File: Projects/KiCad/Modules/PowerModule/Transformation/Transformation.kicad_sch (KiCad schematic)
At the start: 46 parts, among them J1 Conn_01x02_Pin, J2 Conn_01x02_Pin, J3 Conn_01x02_Pin, J4 Conn_01x02_Pin, Q1 TJ8S06M3L, Q2 TJ8S06M3L, Q3 TJ8S06M3L, SW1 SW_SPDT, U1 NJM7812SDL1, U2 NJM7812SDL1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

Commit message: チップ積層セラミックコンデンサをSMD1608に変更
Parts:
- C2, C6, C9: footprint Capacitor_SMD:C_0805_2012Metric_Pad1.18x1.45mm_HandSolder -> Capacitor_SMD:C_0603_1608Metric_Pad1.08x0.95mm_HandSolder
- C3, C4, C5: value 0.33μF -> 10μF; footprint Capacitor_SMD:C_0805_2012Metric_Pad1.18x1.45mm_HandSolder -> Capacitor_SMD:C_0603_1608Metric_Pad1.08x0.95mm_HandSolder
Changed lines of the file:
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@@
       (effects (font (size 1.27 1.27)) (justify left))
     )
-    (property "Value" "0.33μF" (at 52.07 133.985 0)
-      (effects (font (size 1.27 1.27)) (justify left))
-    )
-    (property "Footprint" "Capacitor_SMD:C_0805_2012Metric_Pad1.18x1.45mm_HandSolder" (at 49.2252 135.89 0)
+    (property "Value" "10μF" (at 52.07 133.985 0)
+      (effects (font (size 1.27 1.27)) (justify left))
+    )
+    (property "Footprint" "Capacitor_SMD:C_0603_1608Metric_Pad1.08x0.95mm_HandSolder" (at 49.2252 135.89 0)
       (effects (font (size 1.27 1.27)) hide)
     )
@@
       (effects (font (size 1.27 1.27)) (justify left))
     )
-    (property "Footprint" "Capacitor_SMD:C_0805_2012Metric_Pad1.18x1.45mm_HandSolder" (at 74.6252 135.89 0)
+    (property "Footprint" "Capacitor_SMD:C_0603_1608Metric_Pad1.08x0.95mm_HandSolder" (at 74.6252 135.89 0)
       (effects (font (size 1.27 1.27)) hide)
     )
@@
       (effects (font (size 1.27 1.27)) (justify left))
     )
-    (property "Value" "0.33μF" (at 102.87 133.985 0)
-      (effects (font (size 1.27 1.27)) (justify left))
-    )
-    (property "Footprint" "Capacitor_SMD:C_0805_2012Metric_Pad1.18x1.45mm_HandSolder" (at 100.0252 135.89 0)
+    (property "Value" "10μF" (at 102.87 133.985 0)
+      (effects (font (size 1.27 1.27)) (justify left))
+    )
+    (property "Footprint" "Capacitor_SMD:C_0603_1608Metric_Pad1.08x0.95mm_HandSolder" (at 100.0252 135.89 0)
       (effects (font (size 1.27 1.27)) hide)
     )
@@
       (effects (font (size 1.27 1.27)) (justify left))
     )
-    (property "Value" "0.33μF" (at 151.13 133.985 0)
-      (effects (font (size 1.27 1.27)) (justify left))
-    )
-    (property "Footprint" "Capacitor_SMD:C_0805_2012Metric_Pad1.18x1.45mm_HandSolder" (at 148.2852 135.89 0)
+    (property "Value" "10μF" (at 151.13 133.985 0)
+      (effects (font (size 1.27 1.27)) (justify left))
+    )
+    (property "Footprint" "Capacitor_SMD:C_0603_1608Metric_Pad1.08x0.95mm_HandSolder" (at 148.2852 135.89 0)
       (effects (font (size 1.27 1.27)) hide)
     )
@@
       (effects (font (size 1.27 1.27)) (justify left))
     )
-    (property "Footprint" "Capacitor_SMD:C_0805_2012Metric_Pad1.18x1.45mm_HandSolder" (at 173.6852 135.89 0)
+    (property "Footprint" "Capacitor_SMD:C_0603_1608Metric_Pad1.08x0.95mm_HandSolder" (at 173.6852 135.89 0)
       (effects (font (size 1.27 1.27)) hide)
     )
@@
       (effects (font (size 1.27 1.27)) (justify left))
     )
-    (property "Footprint" "Capacitor_SMD:C_0805_2012Metric_Pad1.18x1.45mm_HandSolder" (at 125.4252 135.89 0)
-      (effects (font (size 1.27 1.27)) hide)
-    )
+    (property "Footprint" "Capacitor_SMD:C_0603_1608Metric_Pad1.08x0.95mm_HandSolder" (at 125.4252 135.89 0)
+      (effects (font (size 1.27 1.27)) hide)
+    )

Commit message: 抵抗の在庫に合わせてサイズを変更
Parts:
- R1, R2: footprint Resistor_SMD:R_0603_1608Metric_Pad0.98x0.95mm_HandSolder -> Resistor_SMD:R_0805_2012Metric_Pad1.20x1.40mm_HandSolder
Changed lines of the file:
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@@
       (effects (font (size 1.27 1.27)) (justify left))
     )
-    (property "Footprint" "Resistor_SMD:R_0603_1608Metric_Pad0.98x0.95mm_HandSolder" (at 55.118 55.88 90)
+    (property "Footprint" "Resistor_SMD:R_0805_2012Metric_Pad1.20x1.40mm_HandSolder" (at 55.118 55.88 90)
       (effects (font (size 1.27 1.27)) hide)
     )
@@
       (effects (font (size 1.27 1.27)) (justify left))
     )
-    (property "Footprint" "Resistor_SMD:R_0603_1608Metric_Pad0.98x0.95mm_HandSolder" (at 46.99 47.752 90)
+    (property "Footprint" "Resistor_SMD:R_0805_2012Metric_Pad1.20x1.40mm_HandSolder" (at 46.99 47.752 90)
       (effects (font (size 1.27 1.27)) hide)
     )

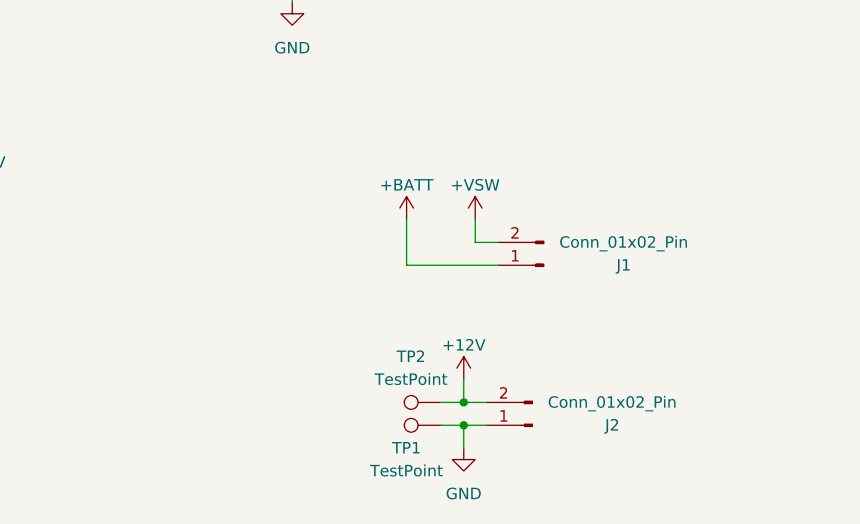
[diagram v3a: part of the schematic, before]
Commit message: コネクタ位置を揃えた
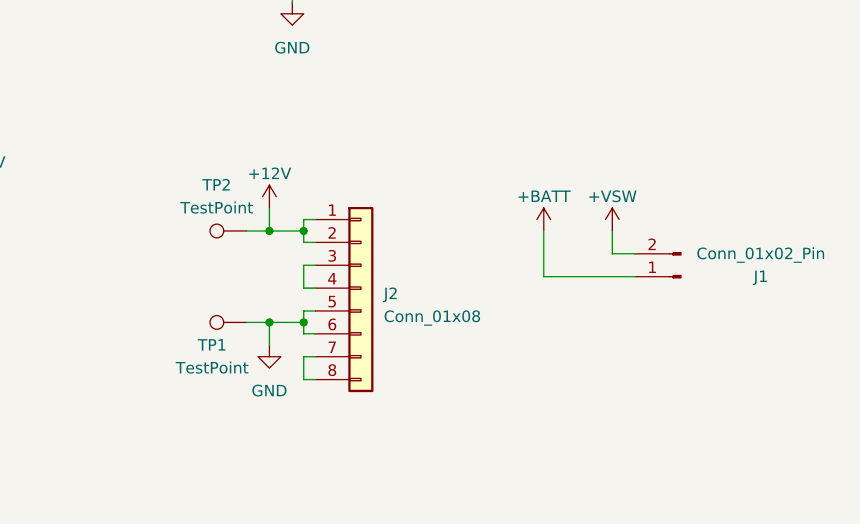
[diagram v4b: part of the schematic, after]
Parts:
- removed J2: Conn_01x02_Pin, Hirose_Connector:Hirose_DF1B, symbol Connector:Conn_01x02_Pin
- added J2: Conn_01x08, Hirose_Connector:Hirose_DF11B-8DP-2DS, symbol Connector_Generic:Conn_01x08
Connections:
- net +12V: now also J2.1 (Pin_1), J2.2 (Pin_2)
- net GND: now also J2.5 (Pin_5), J2.6 (Pin_6)
- new net: J2.3 (Pin_3), J2.4 (Pin_4)
- new net: J2.7 (Pin_7), J2.8 (Pin_8)
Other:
- moved on the sheet: J1, TP1, TP2

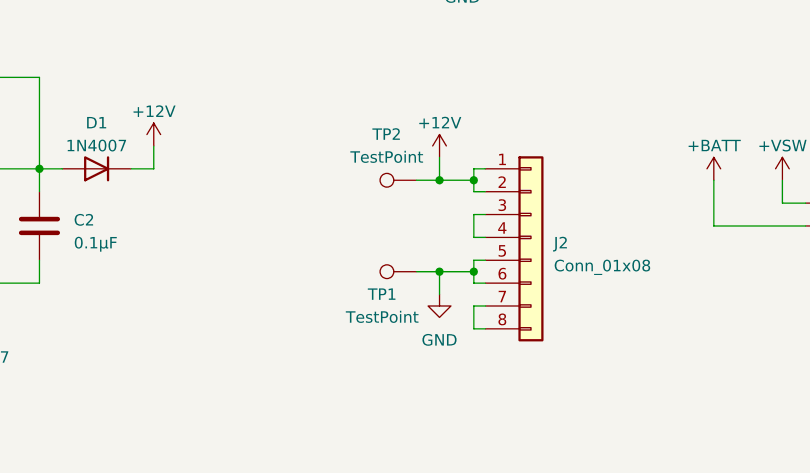
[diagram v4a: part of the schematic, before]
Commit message: コネクタのピン配置を変更
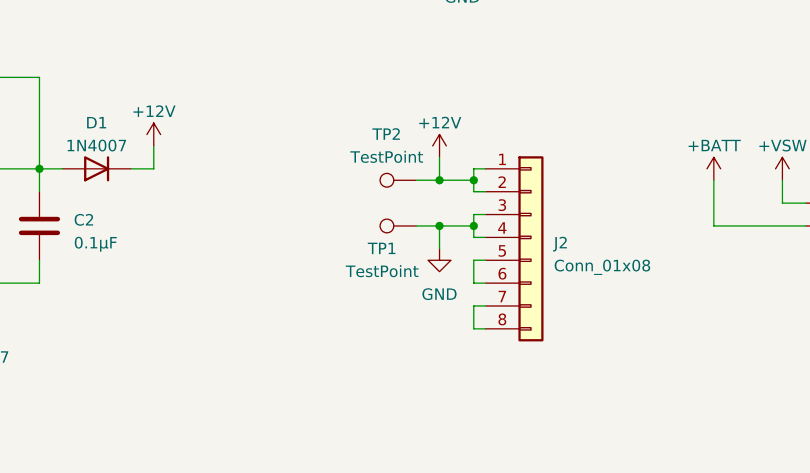
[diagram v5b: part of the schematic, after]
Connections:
- net GND: now also J2.3 (Pin_3), J2.4 (Pin_4); no longer J2.5 (Pin_5), J2.6 (Pin_6)
- new net: J2.5 (Pin_5), J2.6 (Pin_6)
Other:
- moved on the sheet: TP1
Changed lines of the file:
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@@
   (junction (at 154.94 62.23) (diameter 0) (color 0 0 0 0)
   )
+  (junction (at 217.17 132.08) (diameter 0) (color 0 0 0 0)
+  )
   (junction (at 256.54 45.72) (diameter 0) (color 0 0 0 0)
   )
-  (junction (at 220.98 137.16) (diameter 0) (color 0 0 0 0)
-  )
   (junction (at 210.82 33.02) (diameter 0) (color 0 0 0 0)
   )
@@
   (junction (at 245.11 45.72) (diameter 0) (color 0 0 0 0)
   )
+  (junction (at 220.98 132.08) (diameter 0) (color 0 0 0 0)
+  )
   (junction (at 163.83 62.23) (diameter 0) (color 0 0 0 0)
   )
@@
   (junction (at 99.06 125.73) (diameter 0) (color 0 0 0 0)
   )
-  (junction (at 217.17 137.16) (diameter 0) (color 0 0 0 0)
-  )
   (junction (at 179.07 45.72) (diameter 0) (color 0 0 0 0)
   )
@@
     (stroke (width 0) (type default))
   )
+  (wire (pts (xy 220.98 132.08) (xy 220.98 130.81))
+    (stroke (width 0) (type default))
+  )
   (wire (pts (xy 252.73 77.47) (xy 252.73 80.01))
     (stroke (width 0) (type default))
@@
     (stroke (width 0) (type default))
   )
-  (wire (pts (xy 217.17 137.16) (xy 220.98 137.16))
-    (stroke (width 0) (type default))
-  )
   (wire (pts (xy 207.01 78.74) (xy 200.66 78.74))
     (stroke (width 0) (type default))
@@
     (stroke (width 0) (type default))
   )
-  (wire (pts (xy 214.63 137.16) (xy 217.17 137.16))
+  (wire (pts (xy 214.63 132.08) (xy 217.17 132.08))
     (stroke (width 0) (type default))
   )
@@
     (stroke (width 0) (type default))
   )
-  (wire (pts (xy 220.98 135.89) (xy 220.98 137.16))
-    (stroke (width 0) (type default))
-  )
   (wire (pts (xy 219.71 78.74) (xy 219.71 81.28))
     (stroke (width 0) (type default))
@@
     (stroke (width 0) (type default))
   )
-  (wire (pts (xy 220.98 133.35) (xy 220.98 130.81))
-    (stroke (width 0) (type default))
-  )
-  (wire (pts (xy 217.17 139.7) (xy 217.17 137.16))
+  (wire (pts (xy 220.98 133.35) (xy 220.98 132.08))
+    (stroke (width 0) (type default))
+  )
+  (wire (pts (xy 217.17 134.62) (xy 217.17 132.08))
     (stroke (width 0) (type default))
   )
@@
     (stroke (width 0) (type default))
   )
-  (wire (pts (xy 220.98 137.16) (xy 220.98 138.43))
+  (wire (pts (xy 220.98 135.89) (xy 220.98 138.43))
     (stroke (width 0) (type default))
   )
@@
   )
   (wire (pts (xy 255.27 127) (xy 255.27 129.54))
+    (stroke (width 0) (type default))
+  )
+  (wire (pts (xy 217.17 132.08) (xy 220.98 132.08))
     (stroke (width 0) (type default))
   )
@@
     )
   )
-  (symbol (lib_id "Connector:TestPoint") (at 214.63 137.16 90) (unit 1)
+  (symbol (lib_id "Connector:TestPoint") (at 214.63 132.08 90) (unit 1)
     (in_bom yes) (on_board yes) (dnp no)
-    (property "Reference" "TP1" (at 210.82 139.7 90)
-      (effects (font (size 1.27 1.27)))
-    )
-    (property "Value" "TestPoint" (at 210.82 142.24 90)
-      (effects (font (size 1.27 1.27)))
-    )
-    (property "Footprint" "Connector_Pin:Pin_D1.0mm_L10.0mm" (at 214.63 132.08 0)
-      (effects (font (size 1.27 1.27)) hide)
-    )
-    (property "Datasheet" "~" (at 214.63 132.08 0)
+    (property "Reference" "TP1" (at 210.82 134.62 90)
+      (effects (font (size 1.27 1.27)))
+    )
+    (property "Value" "TestPoint" (at 210.82 137.16 90)
+      (effects (font (size 1.27 1.27)))
+    )
+    (property "Footprint" "Connector_Pin:Pin_D1.0mm_L10.0mm" (at 214.63 127 0)
+      (effects (font (size 1.27 1.27)) hide)
+    )
+    (property "Datasheet" "~" (at 214.63 127 0)
       (effects (font (size 1.27 1.27)) hide)
     )
@@
     )
   )
-  (symbol (lib_id "power:GND") (at 217.17 139.7 0) (mirror y) (unit 1)
-    (in_bom yes) (on_board yes) (dnp no) (fields_autoplaced)
-    (property "Reference" "#PWR02" (at 217.17 146.05 0)
-      (effects (font (size 1.27 1.27)) hide)
-    )
-    (property "Value" "GND" (at 217.17 144.78 0)
-      (effects (font (size 1.27 1.27)))
-    )
-    (property "Footprint" "" (at 217.17 139.7 0)
-      (effects (font (size 1.27 1.27)) hide)
-    )
-    (property "Datasheet" "" (at 217.17 139.7 0)
-      (effects (font (size 1.27 1.27)) hide)
-    )
+  (symbol (lib_id "power:GND") (at 217.17 134.62 0) (mirror y) (unit 1)
+    (in_bom yes) (on_board yes) (dnp no) (fields_autoplaced)
+    (property "Reference" "#PWR02" (at 217.17 140.97 0)
+      (effects (font (size 1.27 1.27)) hide)
+    )
+    (property "Value" "GND" (at 217.17 139.7 0)
+      (effects (font (size 1.27 1.27)))
+    )
+    (property "Footprint" "" (at 217.17 134.62 0)
+      (effects (font (size 1.27 1.27)) hide)
+    )
+    (property "Datasheet" "" (at 217.17 134.62 0)
+      (effects (font (size 1.27 1.27)) hide)
+    )

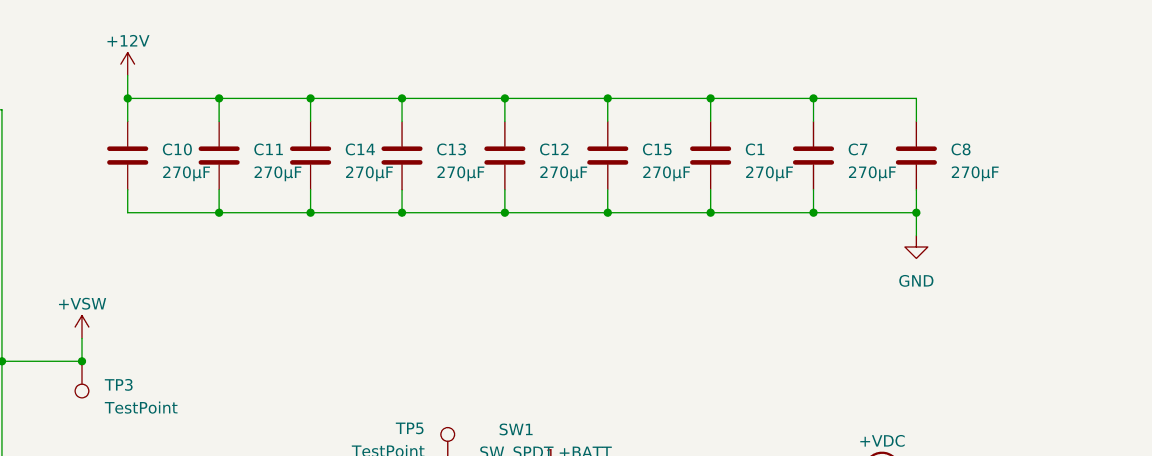
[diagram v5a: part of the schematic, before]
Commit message: バッファコンデンサを表面実装に変更
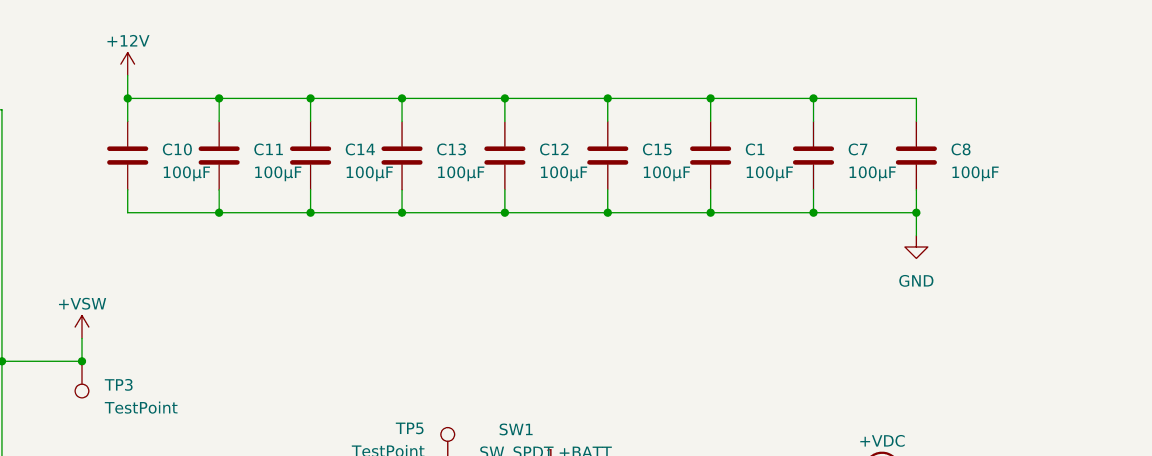
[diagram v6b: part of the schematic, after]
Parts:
- C1, C10, C11, C12, C13, C14, C15, C7, C8: value 270μF -> 100μF; footprint Capacitor_THT:CP_Radial_D10.0mm_P3.50mm -> Capacitor_SMD:CP_Elec_6.3x5.9
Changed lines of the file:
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@@
       (effects (font (size 1.27 1.27)) (justify left))
     )
-    (property "Value" "270μF" (at 203.2 41.275 0)
-      (effects (font (size 1.27 1.27)) (justify left))
-    )
-    (property "Footprint" "Capacitor_THT:CP_Radial_D10.0mm_P3.50mm" (at 200.3552 43.18 0)
+    (property "Value" "100μF" (at 203.2 41.275 0)
+      (effects (font (size 1.27 1.27)) (justify left))
+    )
+    (property "Footprint" "Capacitor_SMD:CP_Elec_6.3x5.9" (at 200.3552 43.18 0)
       (effects (font (size 1.27 1.27)) hide)
     )
@@
       (effects (font (size 1.27 1.27)) (justify left))
     )
-    (property "Value" "270μF" (at 182.88 41.275 0)
-      (effects (font (size 1.27 1.27)) (justify left))
-    )
-    (property "Footprint" "Capacitor_THT:CP_Radial_D10.0mm_P3.50mm" (at 180.0352 43.18 0)
+    (property "Value" "100μF" (at 182.88 41.275 0)
+      (effects (font (size 1.27 1.27)) (justify left))
+    )
+    (property "Footprint" "Capacitor_SMD:CP_Elec_6.3x5.9" (at 180.0352 43.18 0)
       (effects (font (size 1.27 1.27)) hide)
     )
@@
       (effects (font (size 1.27 1.27)) (justify left))
     )
-    (property "Value" "270μF" (at 214.63 41.275 0)
-      (effects (font (size 1.27 1.27)) (justify left))
-    )
-    (property "Footprint" "Capacitor_THT:CP_Radial_D10.0mm_P3.50mm" (at 211.7852 43.18 0)
+    (property "Value" "100μF" (at 214.63 41.275 0)
+      (effects (font (size 1.27 1.27)) (justify left))
+    )
+    (property "Footprint" "Capacitor_SMD:CP_Elec_6.3x5.9" (at 211.7852 43.18 0)
       (effects (font (size 1.27 1.27)) hide)
     )
@@
       (effects (font (size 1.27 1.27)) (justify left))
     )
-    (property "Value" "270μF" (at 172.72 41.275 0)
-      (effects (font (size 1.27 1.27)) (justify left))
-    )
-    (property "Footprint" "Capacitor_THT:CP_Radial_D10.0mm_P3.50mm" (at 169.8752 43.18 0)
+    (property "Value" "100μF" (at 172.72 41.275 0)
+      (effects (font (size 1.27 1.27)) (justify left))
+    )
+    (property "Footprint" "Capacitor_SMD:CP_Elec_6.3x5.9" (at 169.8752 43.18 0)
       (effects (font (size 1.27 1.27)) hide)
     )
@@
       (effects (font (size 1.27 1.27)) (justify left))
     )
-    (property "Value" "270μF" (at 226.06 41.275 0)
-      (effects (font (size 1.27 1.27)) (justify left))
-    )
-    (property "Footprint" "Capacitor_THT:CP_Radial_D10.0mm_P3.50mm" (at 223.2152 43.18 0)
+    (property "Value" "100μF" (at 226.06 41.275 0)
+      (effects (font (size 1.27 1.27)) (justify left))
+    )
+    (property "Footprint" "Capacitor_SMD:CP_Elec_6.3x5.9" (at 223.2152 43.18 0)
       (effects (font (size 1.27 1.27)) hide)
     )
@@
       (effects (font (size 1.27 1.27)) (justify left))
     )
-    (property "Value" "270μF" (at 260.35 41.275 0)
-      (effects (font (size 1.27 1.27)) (justify left))
-    )
-    (property "Footprint" "Capacitor_THT:CP_Radial_D10.0mm_P3.50mm" (at 257.5052 43.18 0)
+    (property "Value" "100μF" (at 260.35 41.275 0)
+      (effects (font (size 1.27 1.27)) (justify left))
+    )
+    (property "Footprint" "Capacitor_SMD:CP_Elec_6.3x5.9" (at 257.5052 43.18 0)
       (effects (font (size 1.27 1.27)) hide)
     )
@@
       (effects (font (size 1.27 1.27)) (justify left))
     )
-    (property "Value" "270μF" (at 193.04 41.275 0)
-      (effects (font (size 1.27 1.27)) (justify left))
-    )
-    (property "Footprint" "Capacitor_THT:CP_Radial_D10.0mm_P3.50mm" (at 190.1952 43.18 0)
+    (property "Value" "100μF" (at 193.04 41.275 0)
+      (effects (font (size 1.27 1.27)) (justify left))
+    )
+    (property "Footprint" "Capacitor_SMD:CP_Elec_6.3x5.9" (at 190.1952 43.18 0)
       (effects (font (size 1.27 1.27)) hide)
     )
@@
       (effects (font (size 1.27 1.27)) (justify left))
     )
-    (property "Value" "270μF" (at 248.92 41.275 0)
-      (effects (font (size 1.27 1.27)) (justify left))
-    )
-    (property "Footprint" "Capacitor_THT:CP_Radial_D10.0mm_P3.50mm" (at 246.0752 43.18 0)
+    (property "Value" "100μF" (at 248.92 41.275 0)
+      (effects (font (size 1.27 1.27)) (justify left))
+    )
+    (property "Footprint" "Capacitor_SMD:CP_Elec_6.3x5.9" (at 246.0752 43.18 0)
       (effects (font (size 1.27 1.27)) hide)
     )
@@
       (effects (font (size 1.27 1.27)) (justify left))
     )
-    (property "Value" "270μF" (at 237.49 41.275 0)
-      (effects (font (size 1.27 1.27)) (justify left))
-    )
-    (property "Footprint" "Capacitor_THT:CP_Radial_D10.0mm_P3.50mm" (at 234.6452 43.18 0)
-      (effects (font (size 1.27 1.27)) hide)
-    )
+    (property "Value" "100μF" (at 237.49 41.275 0)
+      (effects (font (size 1.27 1.27)) (justify left))
+    )
+    (property "Footprint" "Capacitor_SMD:CP_Elec_6.3x5.9" (at 234.6452 43.18 0)
+      (effects (font (size 1.27 1.27)) hide)
+    )
